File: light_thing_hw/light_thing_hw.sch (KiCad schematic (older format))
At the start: 57 parts, among them J1 CONNECTORS, J2 Li-Ion Battery, J3 ADDR_LED_PANEL_1_CONNECTORS, J4 ADDR_LED_PANEL_2_CONNECTORS, J5 MIC_CONN, Q1 MMBF170, SW1 ST_USER_BUTTON1, SW2 ST_RESET_BUTTON, U1 BC832-V1, U2 LSM6DS3, U3 MCP73833T-FCI_UN, U4 LMR62421XMF, U5 LP38511MRX-ADJ_NOPB, U5A1 STM32L452RETx

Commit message: about to change user button
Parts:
- added Q2: BSS83P, Package_TO_SOT_SMD:SOT-23, symbol Transistor_FET:BSS83P
- SW2: footprint Button_Switch_SMD:SW_SPST_CK_RS282G05A3 -> Button_Switch_SMD:SW_SPST_EVPBF
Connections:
- net +3V3: now also Q2.2 (S); no longer J5.2 (Pin_2)
- net MIC_ENABLE: now reaches U5A1.28 (PB2)
- net MIC_ENABLE: now also Q2.1 (G)
- new net MIC_3V3: J5.2 (Pin_2), Q2.3 (D)
- no-connect marks 45 -> 44
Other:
- moved on the sheet: Q1, R10, R11, R12, R13, R14, R2
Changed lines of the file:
@@
 F 0 "SW2" H 8000 1550 50  0000 C CNN
 F 1 "ST_RESET_BUTTON" H 8250 1450 50  0000 C CNN
-F 2 "Button_Switch_SMD:SW_SPST_CK_RS282G05A3" H 8000 1450 50  0001 C CNN
+F 2 "Button_Switch_SMD:SW_SPST_EVPBF" H 8000 1450 50  0001 C CNN
 F 3 "" H 8000 1450 50  0001 C CNN
 	1    8000 1250
@@
 Text GLabel 6450 1650 0    50   Input ~ 0
 BT_RED_LED
+Text GLabel 7100 2650 2    50   Input ~ 0
+I2C2_SCL
 Text GLabel 7100 2750 2    50   Input ~ 0
-I2C2_SCL
-Text GLabel 7100 2850 2    50   Input ~ 0
 I2C2_SDA
-Text GLabel 6350 2850 2    60   Input ~ 0
+Text GLabel 6350 2750 2    60   Input ~ 0
 I2C1_SDA
-Text GLabel 6350 2750 2    60   Input ~ 0
+Text GLabel 6350 2650 2    60   Input ~ 0
 I2C1_SCL
 Wire Wire Line
-	7100 2750 7050 2750
-Wire Wire Line
-	7050 2750 7050 2700
-Wire Wire Line
-	7100 2850 6950 2850
-Wire Wire Line
-	6950 2850 6950 2700
-Wire Wire Line
-	6350 2750 6300 2750
-Wire Wire Line
-	6300 2750 6300 2700
-Wire Wire Line
-	6350 2850 6200 2850
-Wire Wire Line
-	6200 2850 6200 2700
+	7100 2650 7050 2650
+Wire Wire Line
+	7050 2650 7050 2600
+Wire Wire Line
+	7100 2750 6950 2750
+Wire Wire Line
+	6950 2750 6950 2600
+Wire Wire Line
+	6350 2650 6300 2650
+Wire Wire Line
+	6300 2650 6300 2600
+Wire Wire Line
+	6350 2750 6200 2750
+Wire Wire Line
+	6200 2750 6200 2600
 $Comp
 L Device:R R13
 U 1 1 5EF2B2D0
-P 7050 2550
-F 0 "R13" V 7200 2600 50  0000 C CNN
-F 1 "4.7k" V 7300 2600 50  0000 C CNN
-F 2 "Resistor_SMD:R_0603_1608Metric_Pad1.05x0.95mm_HandSolder" V 6980 2550 50  0001 C CNN
-F 3 "~" H 7050 2550 50  0001 C CNN
-	1    7050 2550
+P 7050 2450
+F 0 "R13" V 7200 2500 50  0000 C CNN
+F 1 "4.7k" V 7300 2500 50  0000 C CNN
+F 2 "Resistor_SMD:R_0603_1608Metric_Pad1.05x0.95mm_HandSolder" V 6980 2450 50  0001 C CNN
+F 3 "~" H 7050 2450 50  0001 C CNN
+	1    7050 2450
 	1    0    0    -1
 $EndComp
@@
 L Device:R R12
 U 1 1 5EF67104
-P 6950 2550
-F 0 "R12" V 6850 2600 50  0000 C CNN
-F 1 "4.7k" V 6750 2600 50  0000 C CNN
-F 2 "Resistor_SMD:R_0603_1608Metric_Pad1.05x0.95mm_HandSolder" V 6880 2550 50  0001 C CNN
-F 3 "~" H 6950 2550 50  0001 C CNN
-	1    6950 2550
+P 6950 2450
+F 0 "R12" V 6850 2500 50  0000 C CNN
+F 1 "4.7k" V 6750 2500 50  0000 C CNN
+F 2 "Resistor_SMD:R_0603_1608Metric_Pad1.05x0.95mm_HandSolder" V 6880 2450 50  0001 C CNN
+F 3 "~" H 6950 2450 50  0001 C CNN
+	1    6950 2450
 	1    0    0    -1
 $EndComp
@@
 L Device:R R11
 U 1 1 5EF6E98F
-P 6300 2550
-F 0 "R11" V 6450 2600 50  0000 C CNN
-F 1 "4.7k" V 6550 2600 50  0000 C CNN
-F 2 "Resistor_SMD:R_0603_1608Metric_Pad1.05x0.95mm_HandSolder" V 6230 2550 50  0001 C CNN
-F 3 "~" H 6300 2550 50  0001 C CNN
-	1    6300 2550
+P 6300 2450
+F 0 "R11" V 6450 2500 50  0000 C CNN
+F 1 "4.7k" V 6550 2500 50  0000 C CNN
+F 2 "Resistor_SMD:R_0603_1608Metric_Pad1.05x0.95mm_HandSolder" V 6230 2450 50  0001 C CNN
+F 3 "~" H 6300 2450 50  0001 C CNN
+	1    6300 2450
 	1    0    0    -1
 $EndComp
@@
 L Device:R R10
 U 1 1 5EF6E995
-P 6200 2550
-F 0 "R10" V 6100 2600 50  0000 C CNN
-F 1 "4.7k" V 6000 2600 50  0000 C CNN
-F 2 "Resistor_SMD:R_0603_1608Metric_Pad1.05x0.95mm_HandSolder" V 6130 2550 50  0001 C CNN
-F 3 "~" H 6200 2550 50  0001 C CNN
-	1    6200 2550
+P 6200 2450
+F 0 "R10" V 6100 2500 50  0000 C CNN
+F 1 "4.7k" V 6000 2500 50  0000 C CNN
+F 2 "Resistor_SMD:R_0603_1608Metric_Pad1.05x0.95mm_HandSolder" V 6130 2450 50  0001 C CNN
+F 3 "~" H 6200 2450 50  0001 C CNN
+	1    6200 2450
 	1    0    0    -1
 $EndComp
@@
 L power:+3V3 #PWR0119
 U 1 1 5EF7DA31
-P 6200 2300
-F 0 "#PWR0119" H 6200 2150 50  0001 C CNN
-F 1 "+3V3" H 6200 2440 50  0000 C CNN
-F 2 "" H 6200 2300 50  0001 C CNN
-F 3 "" H 6200 2300 50  0001 C CNN
-	1    6200 2300
-	1    0    0    -1
-$EndComp
-Wire Wire Line
-	6200 2400 6200 2350
-Wire Wire Line
-	6300 2400 6300 2350
-Wire Wire Line
-	6300 2350 6200 2350
-Connection ~ 6200 2350
-Wire Wire Line
-	6200 2350 6200 2300
-Wire Wire Line
-	6950 2400 6950 2350
-Wire Wire Line
-	6950 2350 6300 2350
-Connection ~ 6300 2350
-Wire Wire Line
-	7050 2400 7050 2350
-Wire Wire Line
-	7050 2350 6950 2350
-Connection ~ 6950 2350
+P 6200 2200
+F 0 "#PWR0119" H 6200 2050 50  0001 C CNN
+F 1 "+3V3" H 6200 2340 50  0000 C CNN
+F 2 "" H 6200 2200 50  0001 C CNN
+F 3 "" H 6200 2200 50  0001 C CNN
+	1    6200 2200
+	1    0    0    -1
+$EndComp
+Wire Wire Line
+	6200 2300 6200 2250
+Wire Wire Line
+	6300 2300 6300 2250
+Wire Wire Line
+	6300 2250 6200 2250
+Connection ~ 6200 2250
+Wire Wire Line
+	6200 2250 6200 2200
+Wire Wire Line
+	6950 2300 6950 2250
+Wire Wire Line
+	6950 2250 6300 2250
+Connection ~ 6300 2250
+Wire Wire Line
+	7050 2300 7050 2250
+Wire Wire Line
+	7050 2250 6950 2250
+Connection ~ 6950 2250
 Wire Wire Line
 	3500 5850 3650 5850
@@
 NoConn ~ 10000 2050
 NoConn ~ 10000 2750
-NoConn ~ 10000 3150
 NoConn ~ 10000 3350
 NoConn ~ 10000 3450
@@
 Text GLabel 10000 1850 2    50   Input ~ 0
 BATT_ADC
-Text GLabel 6550 3800 0    50   Input ~ 0
+Text GLabel 6600 3550 0    50   Input ~ 0
 BATT_ADC
 $Comp
 L power:+BATT #PWR07
 U 1 1 5F495415
-P 6800 3450
-F 0 "#PWR07" H 6800 3300 50  0001 C CNN
-F 1 "+BATT" H 6815 3623 50  0000 C CNN
-F 2 "" H 6800 3450 50  0001 C CNN
-F 3 "" H 6800 3450 50  0001 C CNN
-	1    6800 3450
+P 6850 3200
+F 0 "#PWR07" H 6850 3050 50  0001 C CNN
+F 1 "+BATT" H 6865 3373 50  0000 C CNN
+F 2 "" H 6850 3200 50  0001 C CNN
+F 3 "" H 6850 3200 50  0001 C CNN
+	1    6850 3200
 	1    0    0    -1
 $EndComp
@@
 L Device:R R2
 U 1 1 5F4C79E5
-P 6800 3600
-F 0 "R2" H 6650 3650 50  0000 L CNN
-F 1 "1k" H 6650 3550 50  0000 L CNN
-F 2 "Resistor_SMD:R_0603_1608Metric_Pad1.05x0.95mm_HandSolder" V 6730 3600 50  0001 C CNN
-F 3 "~" H 6800 3600 50  0001 C CNN
-	1    6800 3600
+P 6850 3350
+F 0 "R2" H 6700 3400 50  0000 L CNN
+F 1 "1k" H 6700 3300 50  0000 L CNN
+F 2 "Resistor_SMD:R_0603_1608Metric_Pad1.05x0.95mm_HandSolder" V 6780 3350 50  0001 C CNN
+F 3 "~" H 6850 3350 50  0001 C CNN
+	1    6850 3350
 	-1   0    0    1
 $EndComp
@@
 L Device:R R14
 U 1 1 5F4CFECA
-P 6800 4000
-F 0 "R14" H 6870 4046 50  0000 L CNN
-F 1 "1k" H 6870 3955 50  0000 L CNN
-F 2 "Resistor_SMD:R_0603_1608Metric_Pad1.05x0.95mm_HandSolder" V 6730 4000 50  0001 C CNN
-F 3 "~" H 6800 4000 50  0001 C CNN
-	1    6800 4000
+P 6850 3750
+F 0 "R14" H 6920 3796 50  0000 L CNN
+F 1 "1k" H 6920 3705 50  0000 L CNN
+F 2 "Resistor_SMD:R_0603_1608Metric_Pad1.05x0.95mm_HandSolder" V 6780 3750 50  0001 C CNN
+F 3 "~" H 6850 3750 50  0001 C CNN
+	1    6850 3750
 	1    0    0    -1
 $EndComp
@@
 L power:GND #PWR06
 U 1 1 5F4F97CF
-P 6800 4550
-F 0 "#PWR06" H 6800 4300 50  0001 C CNN
-F 1 "GND" H 6800 4400 50  0000 C CNN
-F 2 "" H 6800 4550 50  0001 C CNN
-F 3 "" H 6800 4550 50  0001 C CNN
-	1    6800 4550
+P 6850 4300
+F 0 "#PWR06" H 6850 4050 50  0001 C CNN
+F 1 "GND" H 6850 4150 50  0000 C CNN
+F 2 "" H 6850 4300 50  0001 C CNN
+F 3 "" H 6850 4300 50  0001 C CNN
+	1    6850 4300
 	1    0    0    -1
 $EndComp
@@
 BT_GPIO_3
 Wire Wire Line
-	6800 3750 6800 3800
-Wire Wire Line
-	6550 3800 6800 3800
-Connection ~ 6800 3800
-Wire Wire Line
-	6800 3800 6800 3850
+	6850 3500 6850 3550
+Wire Wire Line
+	6600 3550 6850 3550
+Connection ~ 6850 3550
+Wire Wire Line
+	6850 3550 6850 3600
 $Comp
 L Transistor_FET:MMBF170 Q1
 U 1 1 5F11A036
-P 6700 4350
-F 0 "Q1" H 6905 4396 50  0000 L CNN
-F 1 "MMBF170" H 6905 4305 50  0000 L CNN
-F 2 "Package_TO_SOT_SMD:SOT-23" H 6900 4275 50  0001 L CIN
-F 3 "https://www.diodes.com/assets/Datasheets/ds30104.pdf" H 6700 4350 50  0001 L CNN
-	1    6700 4350
+P 6750 4100
+F 0 "Q1" H 6955 4146 50  0000 L CNN
+F 1 "MMBF170" H 6955 4055 50  0000 L CNN
+F 2 "Package_TO_SOT_SMD:SOT-23" H 6950 4025 50  0001 L CIN
+F 3 "https://www.diodes.com/assets/Datasheets/ds30104.pdf" H 6750 4100 50  0001 L CNN
+	1    6750 4100
 	1    0    0    -1
 $EndComp
 Text GLabel 8700 3550 0    50   Input ~ 0
 BATT_ADC_ENABLE
-Text GLabel 6500 4350 0    50   Input ~ 0
+Text GLabel 6550 4100 0    50   Input ~ 0
 BATT_ADC_ENABLE
 Text Notes 7200 6500 0    50   ~ 0
@@
 $EndComp
 $Comp
-L power:+3V3 #PWR013
-U 1 1 5F0DFE7A
-P 5500 3100
-F 0 "#PWR013" H 5500 2950 50  0001 C CNN
-F 1 "+3V3" V 5515 3273 50  0000 C CNN
-F 2 "" H 5500 3100 50  0001 C CNN
-F 3 "" H 5500 3100 50  0001 C CNN
-	1    5500 3100
-	0    -1   -1   0
-$EndComp
-$Comp
 L power:GND #PWR014
 U 1 1 5F0DFE80
@@
 Text GLabel 5500 3000 0    50   Input ~ 0
 MIC_IN
+Text GLabel 6150 4600 2    50   Input ~ 0
+MIC_ENABLE
+$Comp
+L power:+3V3 #PWR023
+U 1 1 5F2064E5
+P 5900 4850
+F 0 "#PWR023" H 5900 4700 50  0001 C CNN
+F 1 "+3V3" H 5915 5023 50  0000 C CNN
+F 2 "" H 5900 4850 50  0001 C CNN
+F 3 "" H 5900 4850 50  0001 C CNN
+	1    5900 4850
+	1    0    0    -1
+$EndComp
+$Comp
+L Transistor_FET:BSS83P Q2
+U 1 1 5F3B8D0C
+P 6150 4900
+F 0 "Q2" V 6400 5000 50  0000 L CNN
+F 1 "BSS83P" V 6400 4650 50  0000 L CNN
+F 2 "Package_TO_SOT_SMD:SOT-23" H 6350 4825 50  0001 L CIN
+F 3 "http://www.farnell.com/datasheets/1835997.pdf" H 6150 4900 50  0001 L CNN
+	1    6150 4900
+	0    1    1    0
+$EndComp
+Wire Wire Line
+	5900 4850 5900 5000
+Wire Wire Line
+	5900 5000 5950 5000
+Wire Wire Line
+	6150 4600 6150 4700
+Text GLabel 10000 3150 2    50   Input ~ 0
+MIC_ENABLE
+Wire Wire Line
+	6350 5000 6400 5000
+Text GLabel 6400 5000 2    50   Input ~ 0
+MIC_3V3
+Text GLabel 5500 3100 0    50   Input ~ 0
+MIC_3V3
 $EndSCHEMATC

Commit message: hw updates. sent to print
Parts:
- added C19, C20: 220uF, Capacitor_SMD:C_0603_1608Metric_Pad1.05x0.95mm_HandSolder, symbol Device:C_Small
- C7: value 1000uF -> 220uF
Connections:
- net +5V: now also C19.1, C20.1
- net GND: now also C19.2, C20.2
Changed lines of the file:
@@
 I2C2_SDA
-$Comp
-L Device:C_Small C7
-U 1 1 5ED59C90
-P 4500 3200
-F 0 "C7" V 4650 3250 50  0000 L CNN
-F 1 "1000uF" V 4650 2850 50  0000 L CNN
-F 2 "Capacitor_SMD:C_0603_1608Metric_Pad1.05x0.95mm_HandSolder" H 4500 3200 50  0001 C CNN
-F 3 "~" H 4500 3200 50  0001 C CNN
-	1    4500 3200
-	0    -1   -1   0
-$EndComp
 $Comp
 L power:GND #PWR08
 U 1 1 5ED59DA5
-P 4650 3200
-F 0 "#PWR08" H 4650 2950 50  0001 C CNN
-F 1 "GND" H 4655 3027 50  0000 C CNN
-F 2 "" H 4650 3200 50  0001 C CNN
-F 3 "" H 4650 3200 50  0001 C CNN
-	1    4650 3200
+P 4700 3050
+F 0 "#PWR08" H 4700 2800 50  0001 C CNN
+F 1 "GND" H 4705 2877 50  0000 C CNN
+F 2 "" H 4700 3050 50  0001 C CNN
+F 3 "" H 4700 3050 50  0001 C CNN
+	1    4700 3050
 	0    -1   -1   0
 $EndComp
 Wire Wire Line
-	4650 3200 4600 3200
+	4700 3050 4650 3050
 $Comp
 L power:GND #PWR016
@@
 L power:+5V #PWR0113
 U 1 1 5F0C7F22
-P 4400 3200
-F 0 "#PWR0113" H 4400 3050 50  0001 C CNN
-F 1 "+5V" H 4415 3373 50  0000 C CNN
-F 2 "" H 4400 3200 50  0001 C CNN
-F 3 "" H 4400 3200 50  0001 C CNN
-	1    4400 3200
+P 4450 3050
+F 0 "#PWR0113" H 4450 2900 50  0001 C CNN
+F 1 "+5V" H 4465 3223 50  0000 C CNN
+F 2 "" H 4450 3050 50  0001 C CNN
+F 3 "" H 4450 3050 50  0001 C CNN
+	1    4450 3050
 	0    -1   -1   0
 $EndComp
@@
 Text GLabel 5500 3100 0    50   Input ~ 0
 MIC_3V3
+$Comp
+L Device:C_Small C19
+U 1 1 5F158191
+P 4550 3200
+F 0 "C19" V 4700 3250 50  0000 L CNN
+F 1 "220uF" V 4700 2850 50  0000 L CNN
+F 2 "Capacitor_SMD:C_0603_1608Metric_Pad1.05x0.95mm_HandSolder" H 4550 3200 50  0001 C CNN
+F 3 "~" H 4550 3200 50  0001 C CNN
+	1    4550 3200
+	0    -1   -1   0
+$EndComp
+$Comp
+L Device:C_Small C7
+U 1 1 5F1706C5
+P 4550 3050
+F 0 "C7" V 4700 3100 50  0000 L CNN
+F 1 "220uF" V 4700 2700 50  0000 L CNN
+F 2 "Capacitor_SMD:C_0603_1608Metric_Pad1.05x0.95mm_HandSolder" H 4550 3050 50  0001 C CNN
+F 3 "~" H 4550 3050 50  0001 C CNN
+	1    4550 3050
+	0    -1   -1   0
+$EndComp
+$Comp
+L Device:C_Small C20
+U 1 1 5F17C8D1
+P 4550 3350
+F 0 "C20" V 4700 3400 50  0000 L CNN
+F 1 "220uF" V 4700 3000 50  0000 L CNN
+F 2 "Capacitor_SMD:C_0603_1608Metric_Pad1.05x0.95mm_HandSolder" H 4550 3350 50  0001 C CNN
+F 3 "~" H 4550 3350 50  0001 C CNN
+	1    4550 3350
+	0    -1   -1   0
+$EndComp
+Wire Wire Line
+	4450 3200 4450 3050
+Connection ~ 4450 3050
+Wire Wire Line
+	4450 3200 4450 3350
+Connection ~ 4450 3200
+Wire Wire Line
+	4650 3350 4650 3200
+Wire Wire Line
+	4650 3200 4650 3050
+Connection ~ 4650 3200
+Connection ~ 4650 3050
 $EndSCHEMATC

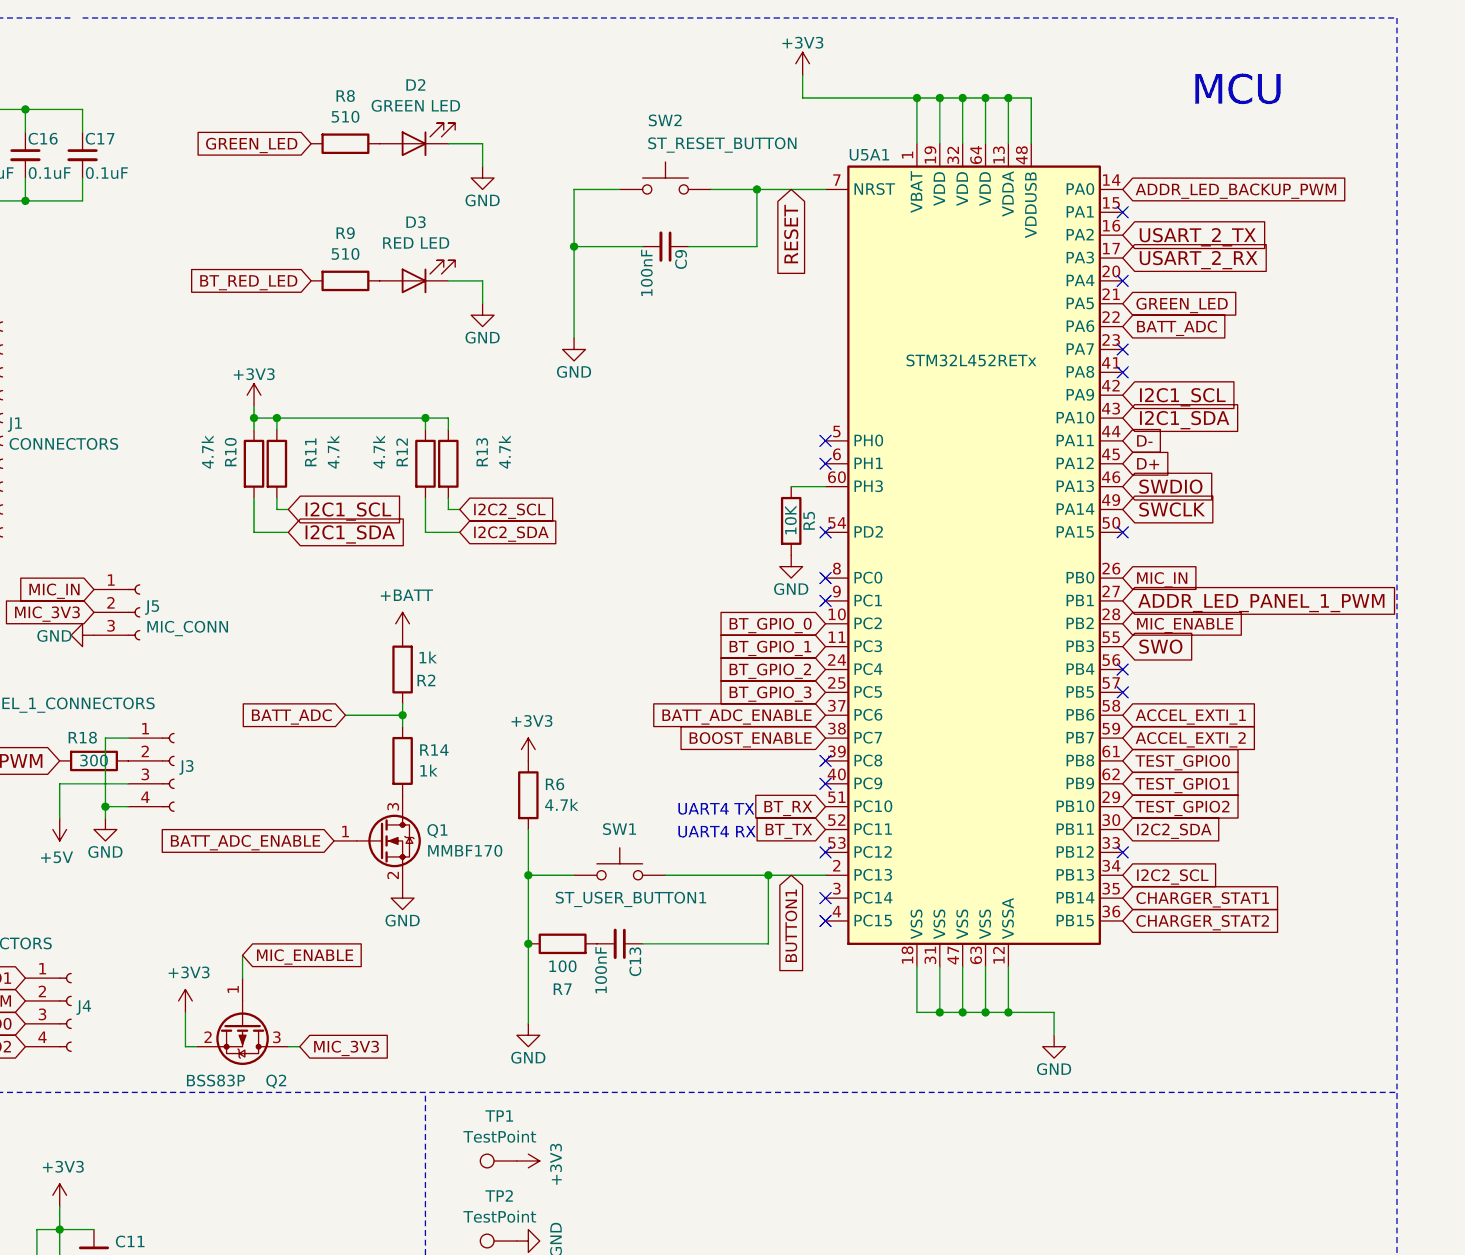
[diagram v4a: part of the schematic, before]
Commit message: moved to STM32L476
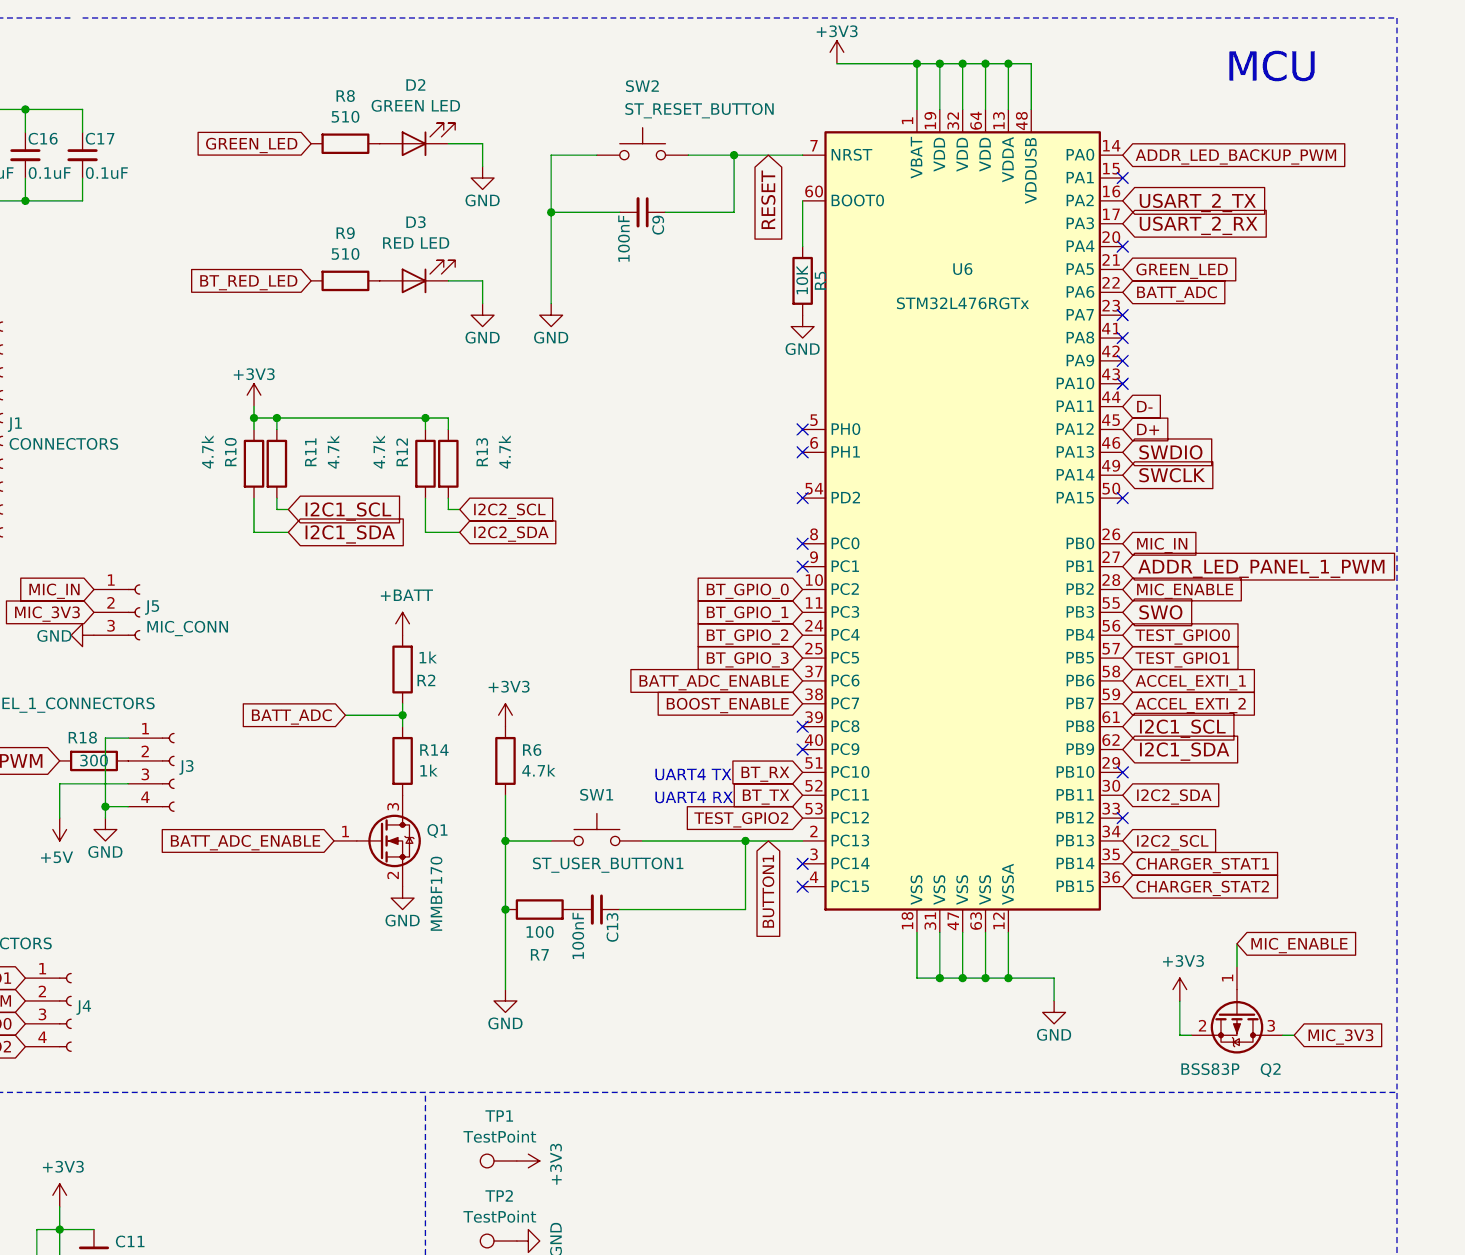
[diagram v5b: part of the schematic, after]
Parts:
- removed U5A1: STM32L452RETx, Package_QFP:LQFP-64-1EP_10x10mm_P0.5mm_EP6.5x6.5mm, symbol MCU_ST_STM32L4:STM32L452RETx
- added U6: STM32L476RGTx, Package_QFP:LQFP-64_10x10mm_P0.5mm, symbol MCU_ST_STM32L4:STM32L476RGTx
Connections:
- net +3V3: now also U6.1 (VBAT), U6.13 (VDDA), U6.19 (VDD), U6.32 (VDD), U6.48 (VDDUSB), U6.64 (VDD)
- net ACCEL_EXTI_1: now also U6.58 (PB6)
- net ACCEL_EXTI_2: now also U6.59 (PB7)
- net ADDR_LED_BACKUP_PWM: now also U6.14 (PA0)
- net ADDR_LED_PANEL_1_PWM: now also U6.27 (PB1)
- net BATT_ADC: now also U6.22 (PA6)
- net BATT_ADC_ENABLE: now also U6.37 (PC6)
- net BOOST_ENABLE: now also U6.38 (PC7)
- net BT_GPIO_0: now also U6.10 (PC2)
- net BT_GPIO_1: now also U6.11 (PC3)
- net BT_GPIO_2: now also U6.24 (PC4)
- net BT_GPIO_3: now also U6.25 (PC5)
- net BT_RX: now also U6.51 (PC10)
- net BT_TX: now also U6.52 (PC11)
- net BUTTON1: now also U6.2 (PC13)
- net CHARGER_STAT1: now also U6.35 (PB14)
- net CHARGER_STAT2: now also U6.36 (PB15)
- net D+: now also U6.45 (PA12)
- net D-: now also U6.44 (PA11)
- net GND: now also U6.12 (VSSA), U6.18 (VSS), U6.31 (VSS), U6.47 (VSS), U6.63 (VSS)
- net GREEN_LED: now also U6.21 (PA5)
- net I2C1_SCL: now also U6.61 (PB8)
- net I2C1_SDA: now also U6.62 (PB9)
- net I2C2_SCL: now also U6.34 (PB13)
- net I2C2_SDA: now also U6.30 (PB11)
- net MIC_ENABLE: now also U6.28 (PB2)
- net MIC_IN: now also U6.26 (PB0)
- net RESET: now also U6.7 (NRST)
- net SWCLK: now also U6.49 (PA14)
- net SWDIO: now also U6.46 (PA13)
- net SWO: now also U6.55 (PB3)
- net TEST_GPIO0: now also U6.56 (PB4)
- net TEST_GPIO1: now also U6.57 (PB5)
- net TEST_GPIO2: now also U6.53 (PC12)
- net USART_2_RX: now also U6.17 (PA3)
- net USART_2_TX: now also U6.16 (PA2)
- net at R5.1: now also U6.60 (BOOT0)
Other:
- moved on the sheet: C13, C9, Q2, R5, R6, R7, SW1, SW2
